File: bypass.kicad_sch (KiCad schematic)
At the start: 8 parts

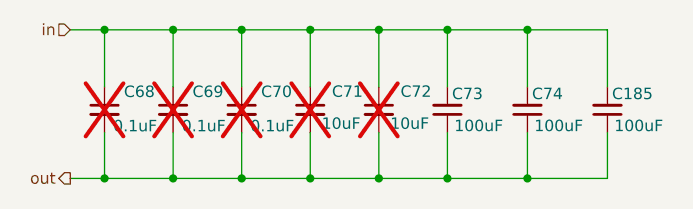
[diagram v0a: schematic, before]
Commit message: finished adding ASICs to schematic. Change VR to single phase 2.8V output
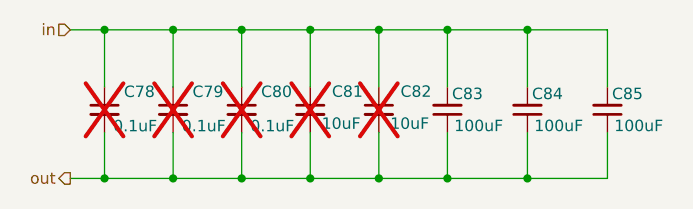
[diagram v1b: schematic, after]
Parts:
- renumbered C68 to C78, C69 to C79, C70 to C80, C71 to C81, C72 to C82, C73 to C83, C74 to C84, C185 to C85

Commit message: switched to THT RPi Pico 2W style. Made 8mm taller.
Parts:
- C83, C84, C85: footprint Capacitor_SMD:C_1206_3216Metric -> Capacitor_SMD:C_0805_2012Metric; DK 1276-1782-1-ND -> 490-GRM21BR60G107ME11KCT-ND; PARTNO CL31A107MQHNNNE -> GRM21BR60G107ME11K; voltage 6.3V -> 4V
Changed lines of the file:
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@@
 			)
 		)
-		(property "Footprint" "Capacitor_SMD:C_1206_3216Metric"
+		(property "Footprint" "Capacitor_SMD:C_0805_2012Metric"
 			(at 175.26 82.55 0)
 			(effects
@@
 			)
 		)
-		(property "voltage" "6.3V"
+		(property "voltage" "4V"
 			(at 179.578 85.852 0)
 			(effects
@@
 			)
 		)
-		(property "PARTNO" "CL31A107MQHNNNE"
+		(property "PARTNO" "GRM21BR60G107ME11K"
 			(at 175.26 82.55 0)
 			(effects
@@
 			)
 		)
-		(property "DK" "1276-1782-1-ND"
+		(property "DK" "490-GRM21BR60G107ME11KCT-ND"
 			(at 175.26 82.55 0)
 			(effects
@@
 			)
 		)
-		(property "Footprint" "Capacitor_SMD:C_1206_3216Metric"
+		(property "Footprint" "Capacitor_SMD:C_0805_2012Metric"
 			(at 166.37 82.55 0)
 			(effects
@@
 			)
 		)
-		(property "voltage" "6.3V"
+		(property "voltage" "4V"
 			(at 170.688 85.852 0)
 			(effects
@@
 			)
 		)
-		(property "PARTNO" "CL31A107MQHNNNE"
+		(property "PARTNO" "GRM21BR60G107ME11K"
 			(at 166.37 82.55 0)
 			(effects
@@
 			)
 		)
-		(property "DK" "1276-1782-1-ND"
+		(property "DK" "490-GRM21BR60G107ME11KCT-ND"
 			(at 166.37 82.55 0)
 			(effects
@@
 			)
 		)
-		(property "Footprint" "Capacitor_SMD:C_1206_3216Metric"
+		(property "Footprint" "Capacitor_SMD:C_0805_2012Metric"
 			(at 157.48 82.55 0)
 			(effects
@@
 			)
 		)
-		(property "voltage" "6.3V"
+		(property "voltage" "4V"
 			(at 161.798 85.852 0)
 			(effects
@@
 			)
 		)
-		(property "PARTNO" "CL31A107MQHNNNE"
+		(property "PARTNO" "GRM21BR60G107ME11K"
 			(at 157.48 82.55 0)
 			(effects
@@
 			)
 		)
-		(property "DK" "1276-1782-1-ND"
+		(property "DK" "490-GRM21BR60G107ME11KCT-ND"
 			(at 157.48 82.55 0)
 			(effects

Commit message: changed all the level shifting diodes to SOD-523 packages for #6
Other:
- title: (none) -> Bitaxe Intel Reference Design System
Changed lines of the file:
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@@
 	(paper "A4")
 	(title_block
-		(date "2025-10-01")
-		(rev "1300xx")
+		(title "Bitaxe Intel Reference Design System")
+		(date "2026-02-09")
+		(rev "1300xxx")
 	)
 	(junction
